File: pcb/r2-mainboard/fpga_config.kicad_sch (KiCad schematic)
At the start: 32 parts, among them U41 XC6SLX-FTG256, U42 W25Q128JVSIQ, X1 33.33MHz

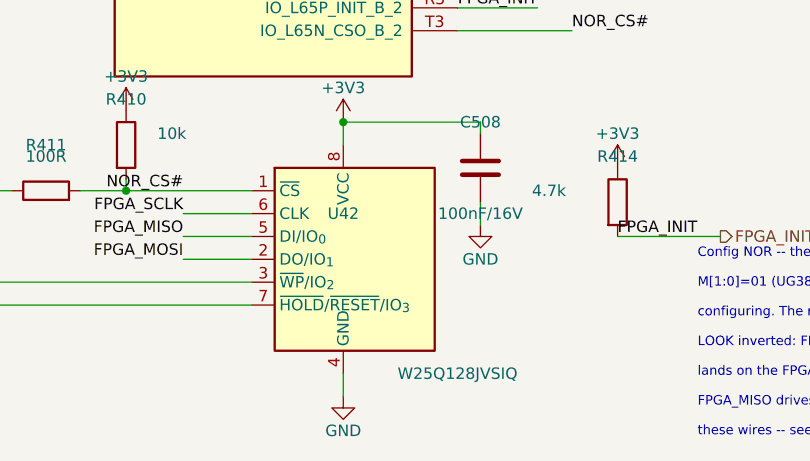
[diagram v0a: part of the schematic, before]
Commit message: change layout and reduce board size + add second usb host only
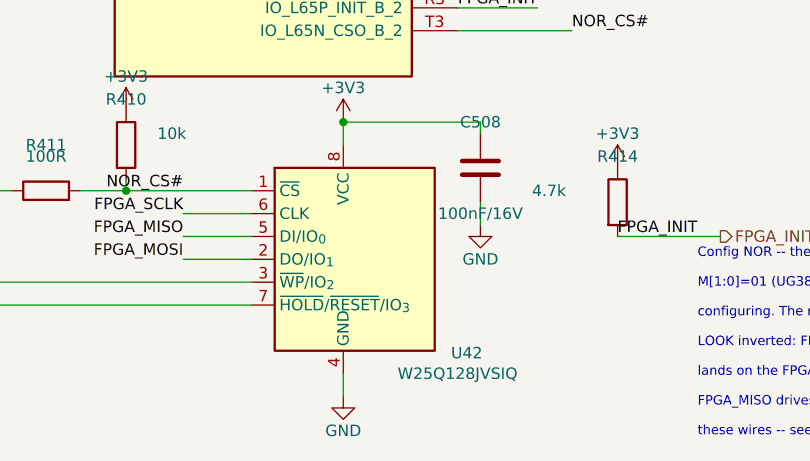
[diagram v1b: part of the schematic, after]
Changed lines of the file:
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@@
 		(dnp no)
 		(property "Reference" "U42"
-			(at 71.12 170.18 0)
+			(at 84.836 185.674 0)
 			(show_name no)
 			(do_not_autoplace no)
